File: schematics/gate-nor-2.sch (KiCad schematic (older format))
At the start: 4 parts, among them Q1 NPN

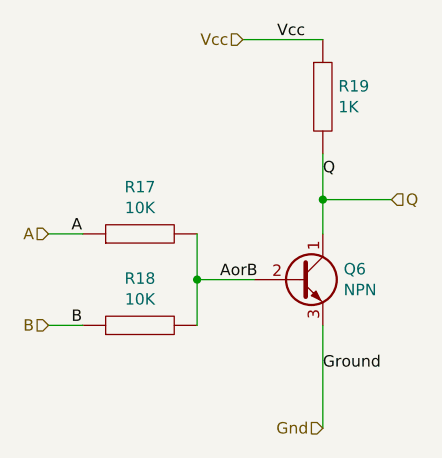
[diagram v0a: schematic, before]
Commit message: Fleshes out basic schematics and some utility software
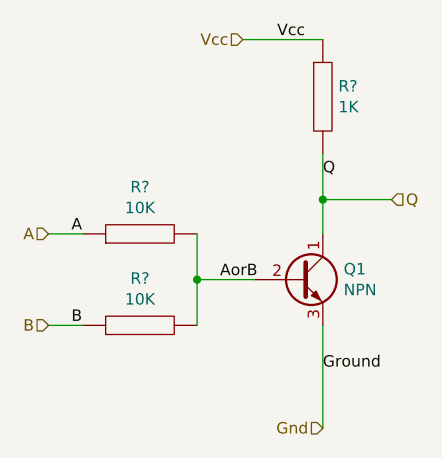
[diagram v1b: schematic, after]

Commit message: Adds a test for the 4-4-1 multiplexer
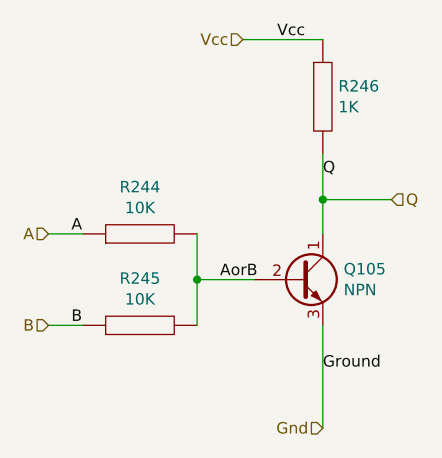
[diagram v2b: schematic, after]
